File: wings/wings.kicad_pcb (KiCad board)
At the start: 2 copper layers, 49 x 12.4 mm, 9 parts, among them U1 VBPW34S, U2 VBPW34S, U3 VBPW34S, U4 VBPW34S

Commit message: big panel, new wing
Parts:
- removed S1: Wings, Custom-wing:fullwing
- removed U1, U2, U3, U4: VBPW34S, VBPW34S:SENSOR-SMD_L4.4-W3.9
- added B1: KXOB25-03X4F-TB, KXOB25-03X4F:KXOB25_AAR, B.Cu at (143.3, 94.1)
- added B2: KXOB25-03X4F-TB, KXOB25-03X4F:KXOB25_AAR, F.Cu at (143.5, 94.3)
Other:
- board size 49 x 12.4 mm -> 55.8 x 17.3 mm

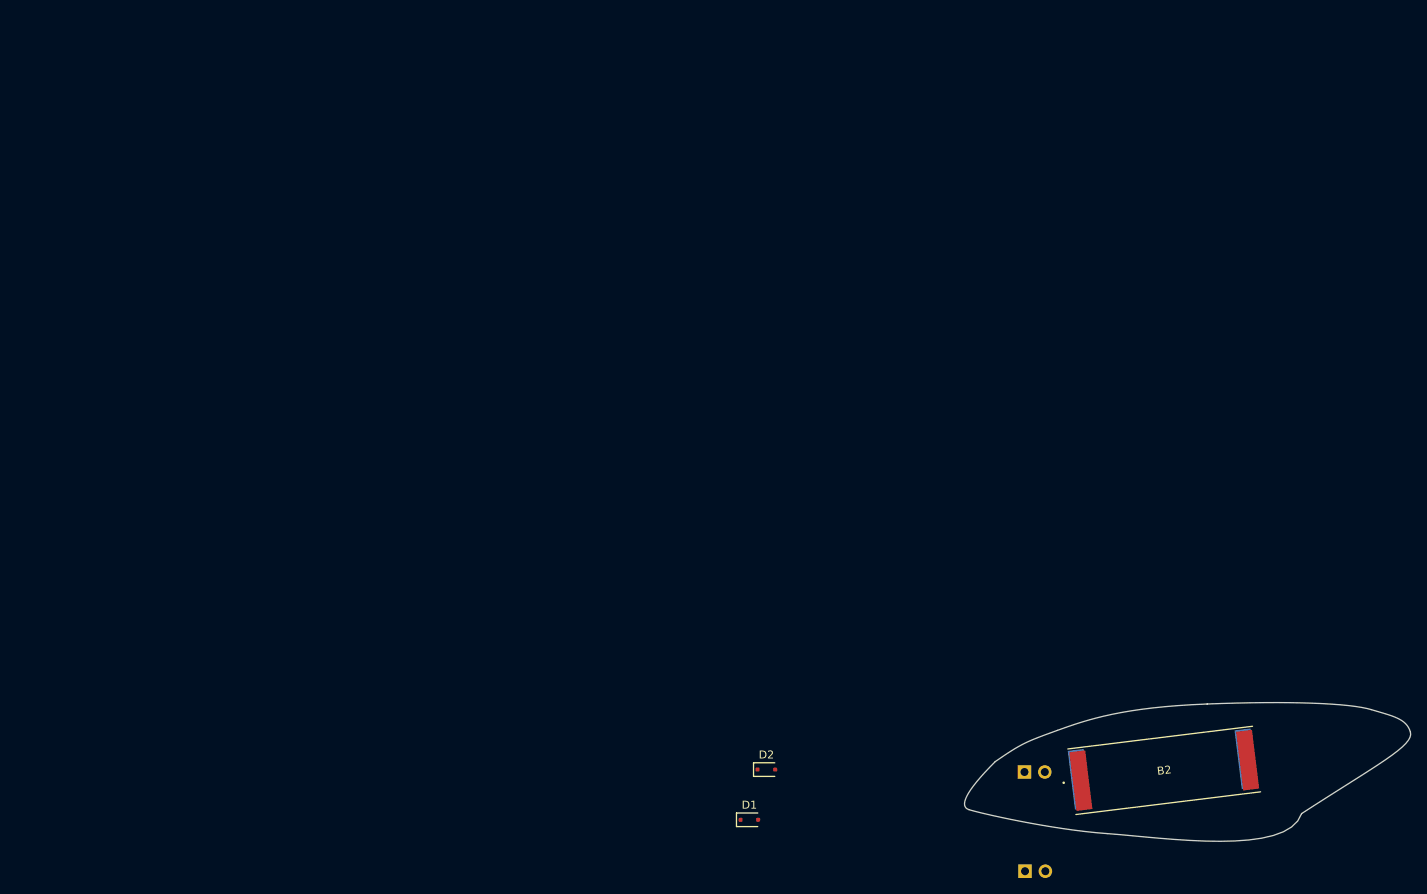
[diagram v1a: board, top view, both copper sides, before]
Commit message: tracks for wings
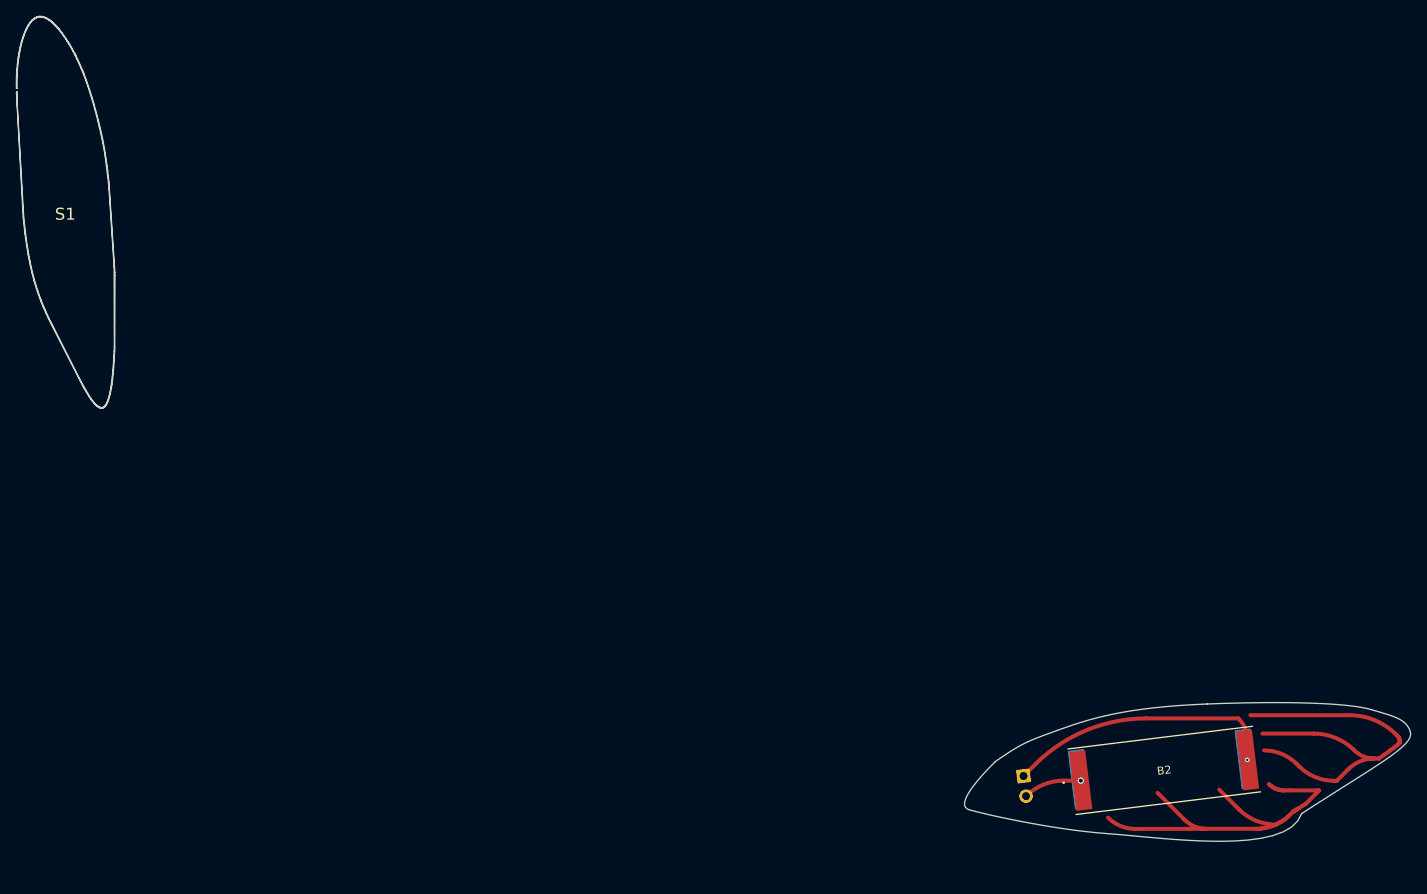
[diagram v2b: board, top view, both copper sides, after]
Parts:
- removed D1, D2: BAT54J, Diode_SMD:D_SOD-323F
- removed TP2: TestPoint_2Pole, Connector_PinSocket_2.54mm:PinSocket_2x01_P2.54mm_Vertical
- added S1: Wings, Custom-wing:fullwing, F.Cu at (2.16, 24.8)
- moved TP1 0.51 mm to (125.9, 95.0), turned to 97 degrees
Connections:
- B1 pad 1: unconnected-(B1-Pad1) -> Net-(B1-Pad1)
- B1 pad 2: unconnected-(B1-Pad2) -> Net-(B1-Pad2)
- B2 pad 1: unconnected-(B2-Pad1) -> Net-(B1-Pad1)
- B2 pad 2: unconnected-(B2-Pad2) -> Net-(B1-Pad2)
- TP1 pad 1: unconnected-(TP1-Pad1) -> Net-(B1-Pad2)
- TP1 pad 2: unconnected-(TP1-Pad2) -> Net-(B1-Pad1)
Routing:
- net (no net): track 0.00 -> 105.5 mm
- net Net-(B1-Pad2): track 0.00 -> 34.5 mm, vias 0 -> 1
- net Net-(B1-Pad1): track 0.00 -> 7.33 mm, vias 0 -> 1

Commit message: rotated terminals
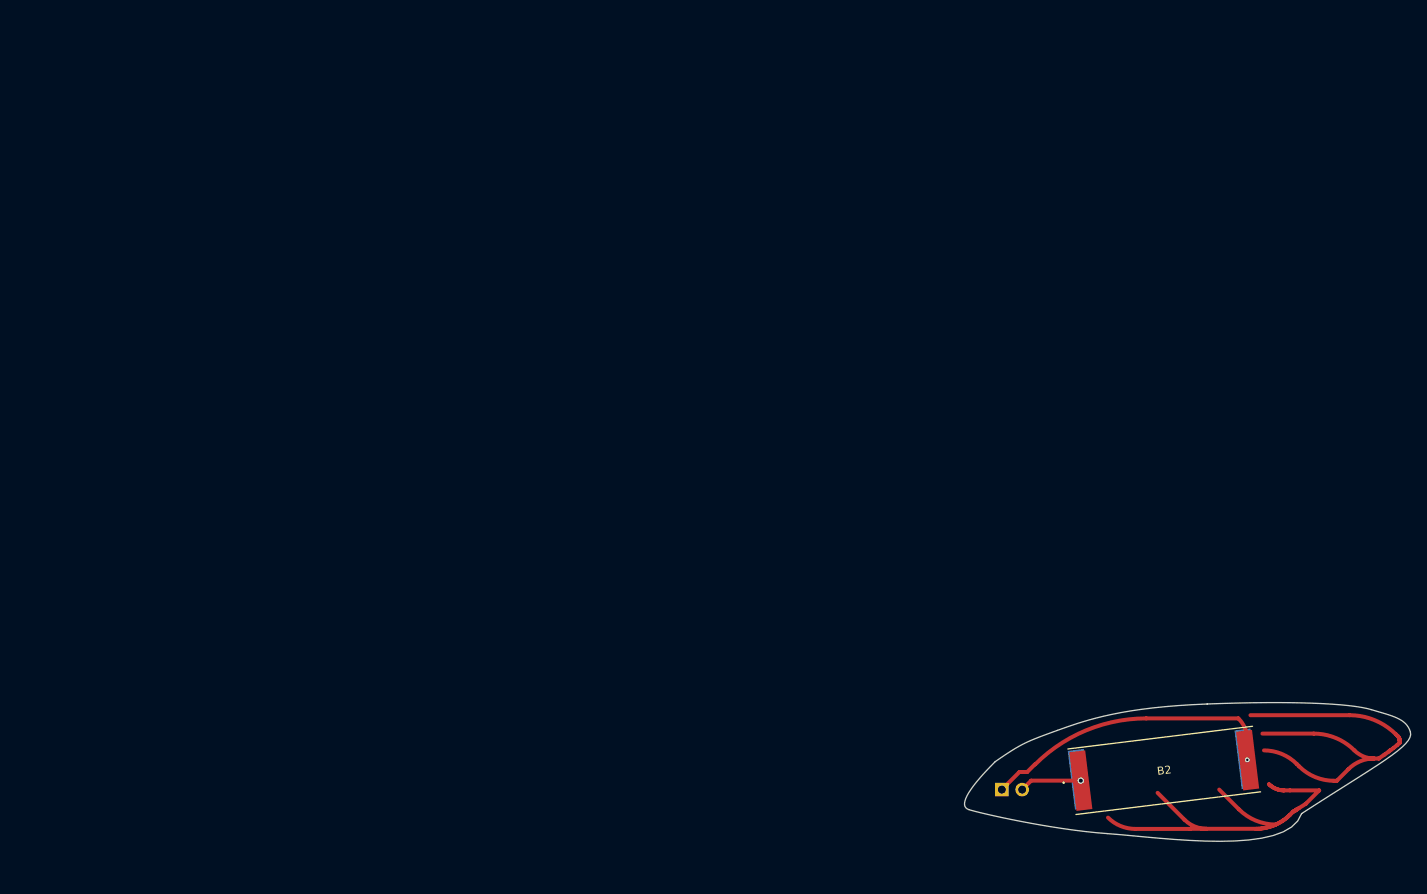
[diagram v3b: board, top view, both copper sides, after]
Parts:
- removed S1: Wings, Custom-wing:fullwing
- moved TP1 3.20 mm to (123.2, 96.7), turned to 180 degrees
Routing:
- net Net-(B1-Pad2): track 34.5 -> 37.9 mm

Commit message: dryfit
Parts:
- moved TP1 1.36 mm to (122.1, 97.5), turned to 170 degrees
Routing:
- net Net-(B1-Pad1): track 7.80 -> 9.53 mm
- net Net-(B1-Pad2): track 37.9 -> 39.3 mm
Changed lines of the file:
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@@
 	(footprint "Connector_PinSocket_2.54mm:PinSocket_2x01_P2.54mm_Vertical"
 		(layer "B.Cu")
-		(at 123.230001 96.700001 180)
+		(at 122.130001 97.500001 170)
 		(descr "Through hole straight socket strip, 2x01, 2.54mm pitch, double rows (from Kicad 4.0.7), script generated")
 		(tags "Through hole socket strip THT 2x01 2.54mm double row")
 		(property "Reference" "TP1"
-			(at -2.44 -2.1 180)
+			(at -2.44 -2.1 170)
 			(layer "B.SilkS")
 			(effects
@@
 		)
 		(property "Value" "TestPoint_2Pole"
-			(at -1.269999 -2.77 180)
+			(at -1.269999 -2.769999 170)
 			(layer "B.Fab")
 			(effects
@@
 		)
 		(property "Datasheet" ""
-			(at 0 0 180)
+			(at 0 0 170)
 			(layer "B.Fab")
 			(hide yes)
@@
 		)
 		(property "Description" "2-polar test point"
-			(at 0 0 180)
+			(at 0 0 170)
 			(layer "B.Fab")
 			(hide yes)
@@
 		)
 		(property "KiLib_Generator" "connector/pin_header_socket"
-			(at 0 0 180)
+			(at 0 0 170)
 			(layer "B.SilkS")
 			(hide yes)
@@
 		)
 		(property "LCSC" "C492401"
-			(at 0 0 0)
+			(at 0 0 350)
 			(unlocked yes)
 			(layer "B.Fab")
@@
 		(duplicate_pad_numbers_are_jumpers no)
 		(fp_line
-			(start 1.33 -1.270001)
-			(end 1.33 -1.329999)
+			(start 1.33 -1.27)
+			(end 1.330001 -1.329998)
 			(stroke
 				(width 0.12)
@@
 		)
 		(fp_line
-			(start 1.329999 1.33)
+			(start 1.329998 1.330001)
 			(end 1.33 0)
 			(stroke
@@
 		(fp_line
 			(start 0 1.33)
-			(end 1.329999 1.33)
+			(end 1.329998 1.330001)
 			(stroke
 				(width 0.12)
@@
 		(fp_line
 			(start -1.27 -1.27)
-			(end 1.33 -1.270001)
+			(end 1.33 -1.27)
 			(stroke
 				(width 0.12)
@@
 		)
 		(fp_line
-			(start -1.270002 1.33)
+			(start -1.270002 1.329999)
 			(end -1.27 -1.27)
 			(stroke
@@
 		)
 		(fp_line
-			(start -3.87 1.33)
-			(end -1.270002 1.33)
+			(start -3.87 -1.329999)
+			(end 1.330001 -1.329998)
 			(stroke
 				(width 0.12)
@@
 		)
 		(fp_line
-			(start -3.87 1.33)
-			(end -3.87 -1.33)
+			(start -3.869999 1.33)
+			(end -1.270002 1.329999)
 			(stroke
 				(width 0.12)
@@
 		)
 		(fp_line
-			(start -3.87 -1.33)
-			(end 1.33 -1.329999)
+			(start -3.869999 1.33)
+			(end -3.87 -1.329999)
 			(stroke
 				(width 0.12)
@@
 		(fp_line
 			(start 1.770001 -1.769999)
-			(end -4.309999 -1.77)
+			(end -4.31 -1.77)
 			(stroke
 				(width 0.05)
@@
 		)
 		(fp_line
-			(start -4.309999 -1.77)
+			(start -4.31 -1.77)
 			(end -4.31 1.769999)
 			(stroke
@@
 		(fp_line
 			(start 1.27 -1.27)
-			(end -3.809999 -1.269999)
+			(end -3.809999 -1.27)
 			(stroke
 				(width 0.1)
@@
 		)
 		(fp_line
-			(start -3.809999 -1.269999)
+			(start -3.809999 -1.27)
 			(end -3.81 1.269999)
 			(stroke
@@
 		)
 		(fp_text user "${REFERENCE}"
-			(at -1.27 0.000001 180)
+			(at -1.27 0.000002 170)
 			(layer "B.Fab")
 			(effects
@@
 		)
 		(pad "1" thru_hole rect
-			(at 0 0 180)
+			(at 0 0 170)
 			(size 1.7 1.7)
 			(drill 1)
@@
 		)
 		(pad "2" thru_hole circle
-			(at -2.540001 0.000001 180)
+			(at -2.540001 0.000001 170)
 			(size 1.7 1.7)
 			(drill 1)
@@
 	)
 	(segment
-		(start 126.89002 95.579982)
+		(start 126.59002 95.579982)
 		(end 133.101728 95.579982)
 		(width 0.5)
@@
 	)
 	(segment
-		(start 125.770002 96.7)
-		(end 126.89002 95.579982)
+		(start 124.970002 97.5)
+		(end 124.670002 97.5)
+		(width 0.5)
+		(layer "F.Cu")
+		(net "Net-(B1-Pad1)")
+	)
+	(segment
+		(start 124.670002 97.5)
+		(end 126.59002 95.579982)
 		(width 0.5)
 		(layer "F.Cu")
@@
 	)
 	(segment
+		(start 126.4 94.5)
+		(end 127.349589 93.550411)
+		(width 0.5)
+		(layer "F.Cu")
+		(net "Net-(B1-Pad2)")
+	)
+	(segment
+		(start 122.430001 97.500001)
+		(end 125.430002 94.5)
+		(width 0.5)
+		(layer "F.Cu")
+		(net "Net-(B1-Pad2)")
+	)
+	(segment
 		(start 141.277625 87.8)
 		(end 152.8 87.8)
@@
 	)
 	(segment
-		(start 123.230001 96.700001)
-		(end 125.430002 94.5)
-		(width 0.5)
-		(layer "F.Cu")
-		(net "Net-(B1-Pad2)")
-	)
-	(segment
-		(start 126.4 94.5)
-		(end 127.349589 93.550411)
-		(width 0.5)
-		(layer "F.Cu")
+		(start 122.130001 97.500001)
+		(end 122.430001 97.500001)
+		(width 0.5)
+		(layer "F.Cu")

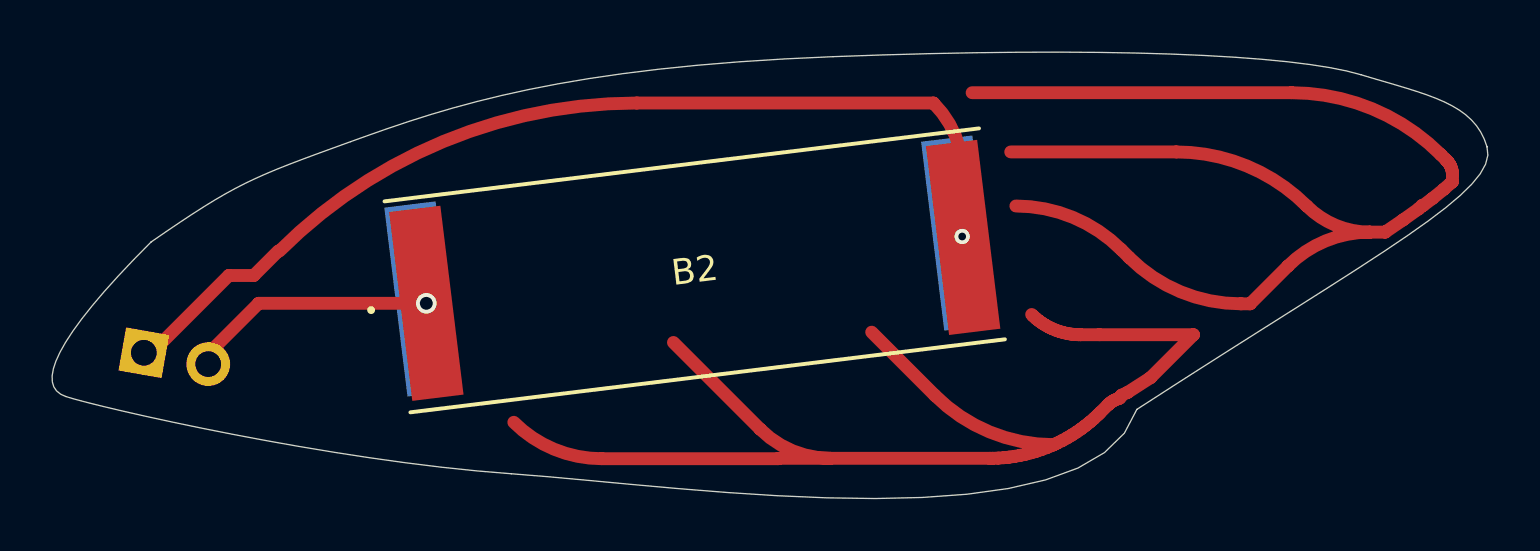
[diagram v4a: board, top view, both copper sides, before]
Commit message: Created 3D models of main body board, wings and double sided wings. added 3D models for solar cells
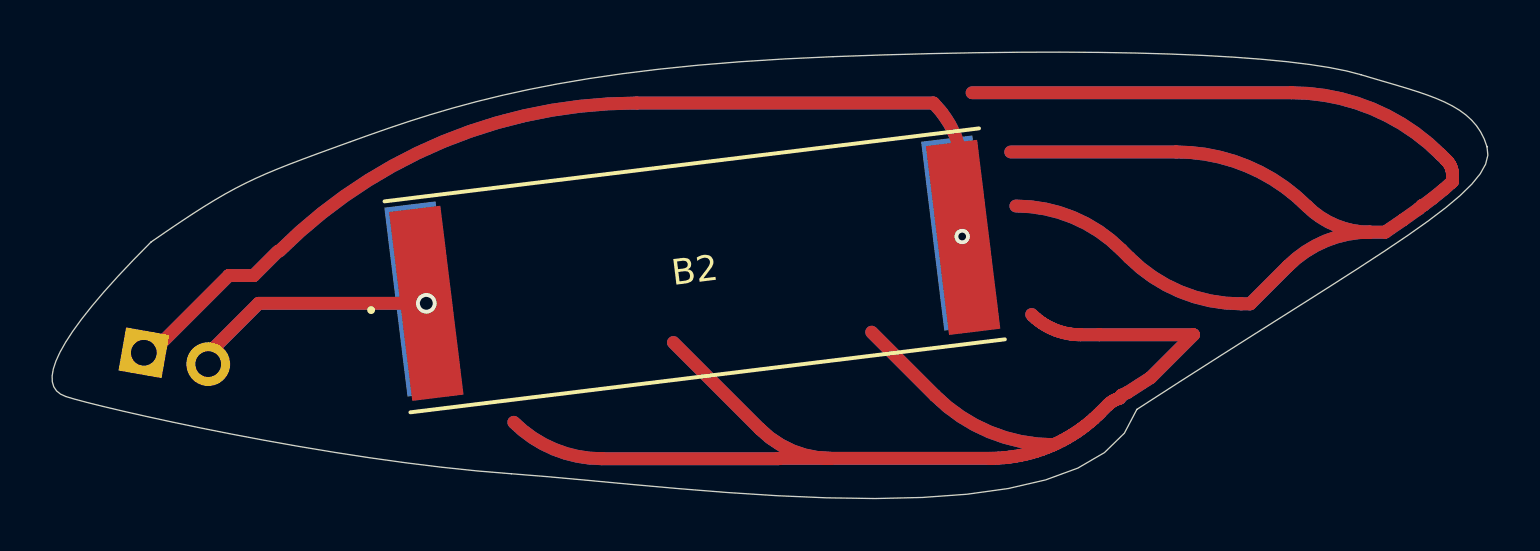
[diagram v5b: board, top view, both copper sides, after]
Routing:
- net Net-(B1-Pad2): track 39.3 -> 132.9 mm
- net (no net): track 105.5 -> 156.8 mm
- net Net-(B1-Pad1): track 9.53 -> 19.1 mm
